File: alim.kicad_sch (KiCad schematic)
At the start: 13 parts

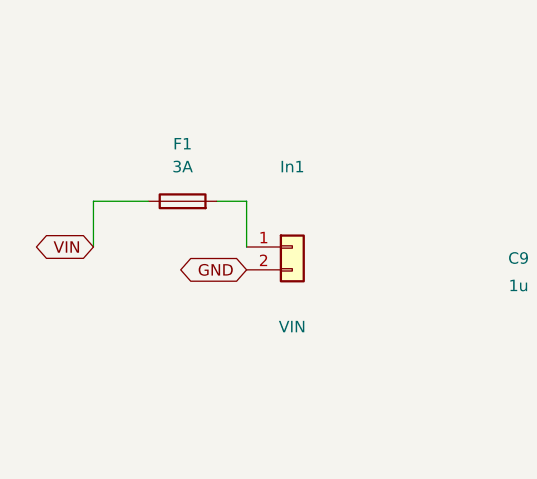
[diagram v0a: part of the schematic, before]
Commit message: Retire la barriere d'isolation primaire/secondaire (secondaire non isole du primaire dans le montage final)
Decision utilisateur du 2026-10-25 : le secondaire de puissance (VOUT_N/
VOUT_P) ne sera plus flottant ni isole galvaniquement du primaire. La
regle .kicad_dru barriere_primaire_secondaire est retiree (commentee,
pas supprimee), la classe de nets SEC est conservee a titre
organisationnel dans KICAD-HT.kicad_pro. Seule la barriere controle
(C2000) <-> puissance reste une isolation reelle. 00-intention-conception.md,
README.md et doc/plan-isolation-4couches.md mis a jour (section 20bis).
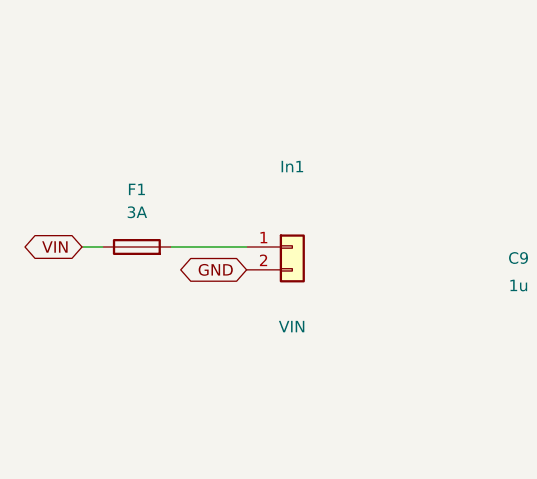
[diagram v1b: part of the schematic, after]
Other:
- moved on the sheet: F1
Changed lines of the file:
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@@
 	(wire
 		(pts
-			(xy 53.34 45.72) (xy 53.34 50.8)
-		)
-		(stroke
-			(width 0)
-			(type default)
-		)
-	)
-	(wire
-		(pts
-			(xy 42.418 45.72) (xy 36.322 45.72)
+			(xy 37.338 50.8) (xy 35.052 50.8)
 		)
 		(stroke
@@
 	(wire
 		(pts
-			(xy 50.038 45.72) (xy 53.34 45.72)
+			(xy 44.958 50.8) (xy 53.34 50.8)
 		)
 		(stroke
@@
 	(wire
 		(pts
-			(xy 36.322 45.72) (xy 36.322 50.8)
-		)
-		(stroke
-			(width 0)
-			(type default)
-		)
-	)
-	(wire
-		(pts
 			(xy 106.68 45.72) (xy 106.68 50.8)
 		)
@@
 	(global_label "VIN"
 		(shape bidirectional)
-		(at 36.322 50.8 180)
+		(at 35.052 50.8 180)
 		(fields_autoplaced yes)
 		(effects
@@
 		)
 		(property "Intersheetrefs" "${INTERSHEET_REFS}"
-			(at 36.322 50.8 0)
+			(at 35.052 50.8 0)
 			(hide yes)
 			(show_name no)
@@
 	(symbol
 		(lib_id "Device:Fuse")
-		(at 46.228 45.72 90)
+		(at 41.148 50.8 90)
 		(unit 1)
 		(body_style 1)
@@
 		(fields_autoplaced yes)
 		(property "Reference" "F1"
-			(at 46.228 39.37 90)
+			(at 41.148 44.45 90)
 			(show_name no)
 			(do_not_autoplace no)
@@
 		)
 		(property "Value" "3A"
-			(at 46.228 41.91 90)
+			(at 41.148 46.99 90)
 			(show_name no)
 			(do_not_autoplace no)
@@
 		)
 		(property "Footprint" "Fuse:Fuseholder_Clip-5x20mm_Littelfuse_111_Lateral_P18.80x5.00mm_D1.17mm_Horizontal"
-			(at 46.228 47.498 90)
+			(at 41.148 52.578 90)
 			(hide yes)
 			(show_name no)
@@
 		)
 		(property "Datasheet" ""
-			(at 46.228 45.72 0)
+			(at 41.148 50.8 0)
 			(hide yes)
 			(show_name no)
@@
 		)
 		(property "Description" "Fuse"
-			(at 46.228 45.72 0)
-			(hide yes)
-			(show_name no)
+			(at 41.148 50.8 0)
+			(hide yes)
+			(show_name no)
